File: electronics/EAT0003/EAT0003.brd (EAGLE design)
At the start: 29.4 x 62.8 mm, 42 parts, among them IC1 LM2596S, J1 CONN-OSTTE1201X4, J2 CONN-RECT-16PIN-2ROWSIDE, Q1 MMBT3904, U1 24AA014, U2 MIC5205, U3 LM317KTTR, U4 H11F1SM

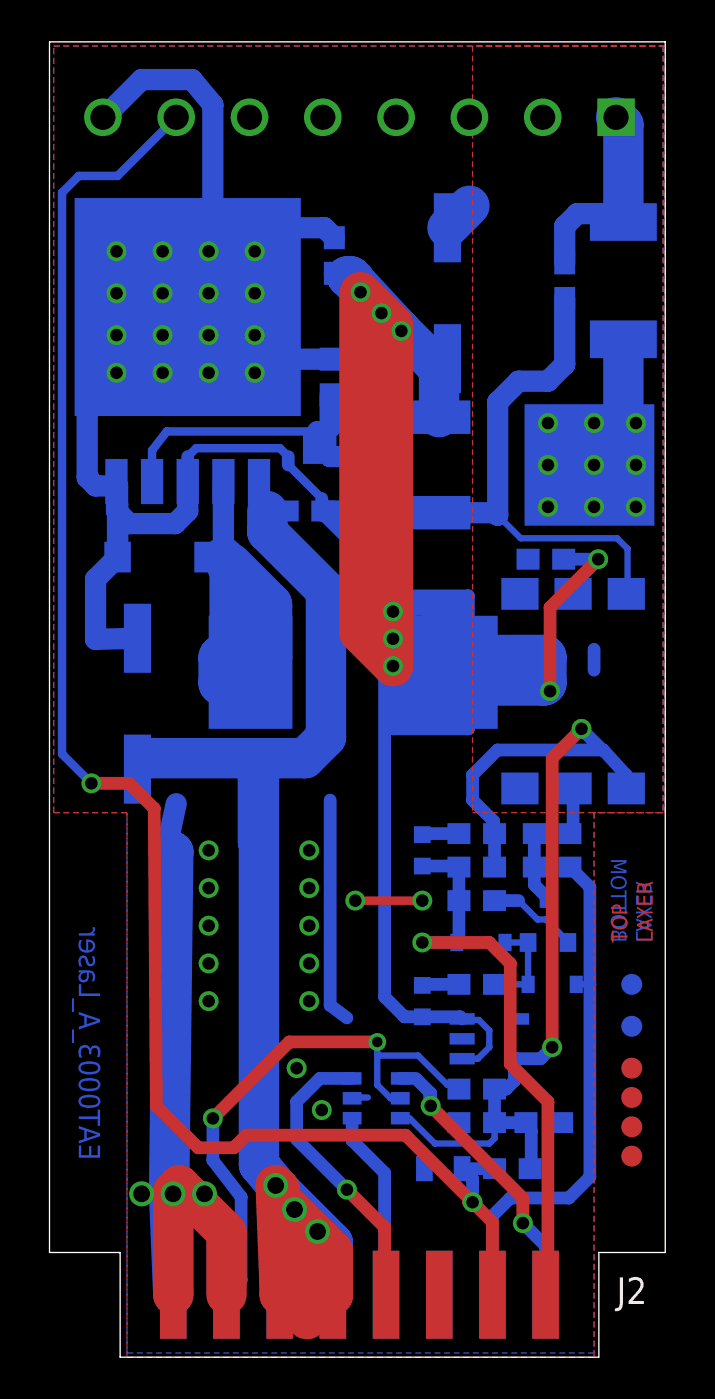
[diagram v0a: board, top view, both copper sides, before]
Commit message: Laser Schematic + PCB Update
Added 30 mm fan mounts + connector
Changed values to suit mods on prototype
Added switchmode PSU enable line to global enable line to stop current
flowing
Added more TODO:'s to schematic
Added copper pours on both sides of PCB
Un mirrored PCB
Added logo's, part number, fiducials back in
Changed LM317 to correct footprint
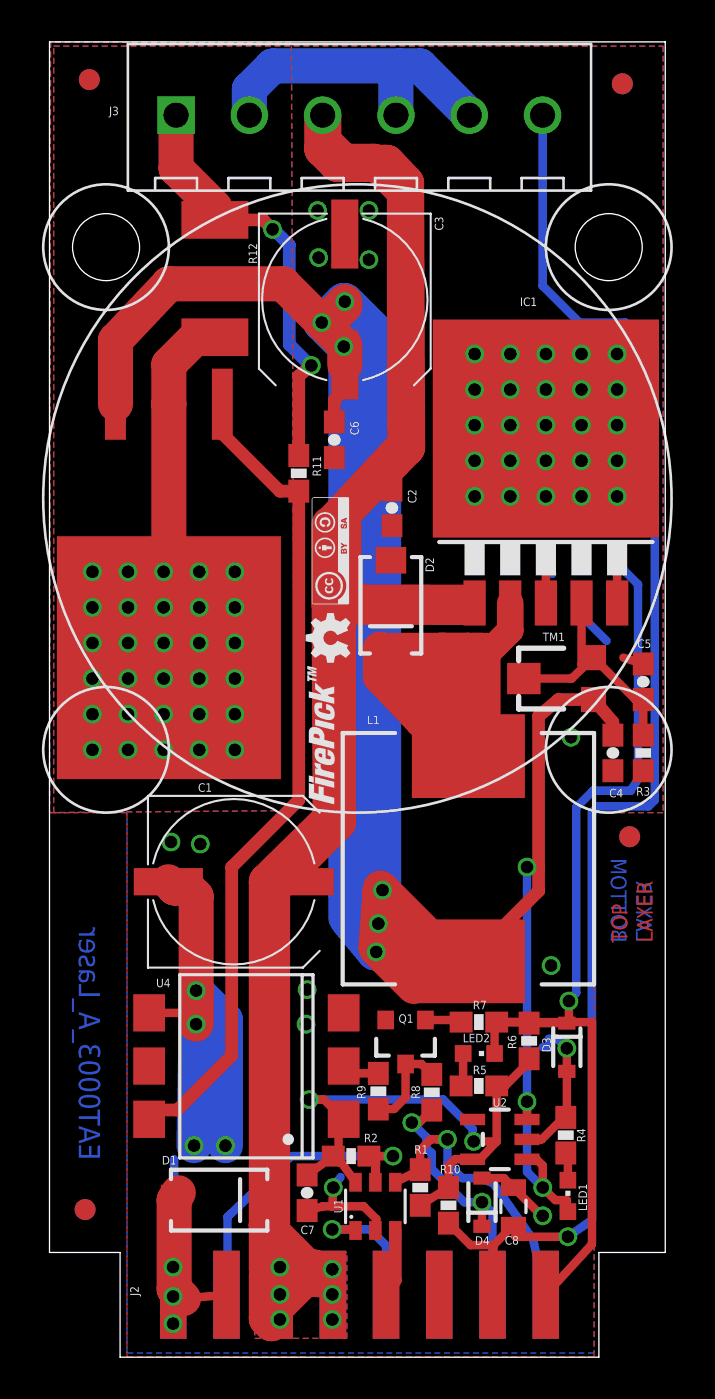
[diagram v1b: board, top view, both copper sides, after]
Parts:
- removed J1: CONN-OSTTE1201X4, FirePick:CONN-OSTTE1201X4
- added FAN1: FAN_30MM, fan:FAN_30MM_X_30MM
- added FID7, FID8: FIDUCIAL1X2, SparkFun-Aesthetics:FIDUCIAL-1X2
- added J3: CONN-RECT-6PIN, CONN_FPD:CONN-OSTTE_6PIN
- added LOGO1, LOGO5: LOGO-CC-BY-SASMALL, FirePick:LOGO-CC-BY-SA-SMALL
- added LOGO2, LOGO6: LOGO-FIREPICKSMALL, FirePick:LOGO-FIREPICK-SMALL
- added LOGO3, LOGO4: LOGO-OSHWSMALL, FirePick:LOGO-OSHW-SMALL
- R4, R5: value 1K 1% -> 10K 1%
- R6: value 10K 1% -> 1K 1%
- U3: device SparkFun-PowerIC:V-REG_DPACK -> LM317:D2PAK-3
- moved FID4 57.6 mm to (1.70, 61.0)
- moved FID5 48.4 mm to (27.1, 60.8)
- moved FID2 28.2 mm to (1.50, 7.05)
- moved C4 27.2 mm to (26.7, 28.9), flipped to the top, turned to 270 degrees
- moved FID3 26.4 mm to (1.50, 7.05)
- moved U4 23.7 mm to (9.20, 13.9), flipped to the top, turned to 90 degrees
- moved C5 20.9 mm to (28.1, 32.2), flipped to the top
- moved R12 19.5 mm to (7.70, 51.5), flipped to the top
- moved U3 19.3 mm to (5.50, 34.9), flipped to the top, turned to 180 degrees
- moved IC1 18.1 mm to (23.5, 41.8), flipped to the top
- moved R3 17.4 mm to (28.1, 28.9), flipped to the top, turned to 90 degrees
- moved D1 17.1 mm to (7.90, 7.50), flipped to the top, turned to 0 degrees
- moved R11 15.7 mm to (11.7, 42.2), flipped to the top
- moved R9 14.8 mm to (15.5, 12.7), flipped to the top, turned to 90 degrees
- moved TM1 14.7 mm to (23.9, 32.4), flipped to the top, turned to 90 degrees
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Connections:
- net !ENABLE: now also IC1.5
- net AIN: now also J3.6; no longer J1.7
- net GND: now also J3.2, J3.4, J3.5; no longer IC1.5, J1.2, J1.8
- net LASER_POS: now also J3.1; no longer J1.1
- net N$7: now also U3.2, U3.PAD; no longer U3.4
- net V+: now also J3.3
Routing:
- net V+: track 90.7 -> 157.0 mm, vias 3 -> 6
- net GND: track 136.1 -> 76.6 mm, vias 33 -> 46
- net +9V: track 167.6 -> 213.6 mm, vias 8 -> 9
- net !ENABLE: track 28.3 -> 49.7 mm, vias 1 -> 2
- net 5V: track 46.4 -> 29.3 mm
- net N$4: track 24.4 -> 40.1 mm
- net DOUT: track 25.0 -> 12.7 mm, vias 0 -> 2
- net SDA: track 14.1 -> 3.20 mm, vias 1 -> 0
- net LASER_POS: track 9.91 -> 20.6 mm, vias 0 -> 2
- net N$3: track 25.8 -> 36.1 mm
- net A0: track 26.6 -> 16.4 mm, vias 2 -> 1
- net N$7: track 6.89 -> 16.7 mm, vias 9 -> 30
- net AIN: track 79.3 -> 69.7 mm, vias 2 -> 1
- net N$23: track 18.8 -> 12.7 mm
- net A1: track 16.8 -> 14.0 mm, vias 2 -> 1
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- added copper zone on layer 16, net N$7
- added copper zone on layer 1, net V+
- added copper zone on layer 16, net V+
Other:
- board text added: "LASER"
- board text added: "V SUPPLY"
- board text removed: "1A"
- board text removed: "A2"
- board text removed: "B1"
- board text removed: "B2"
- board text removed: "MOSFET"
- board text removed: "STEPPER MOTOR"
